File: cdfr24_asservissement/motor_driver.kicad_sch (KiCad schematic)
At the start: 14 parts

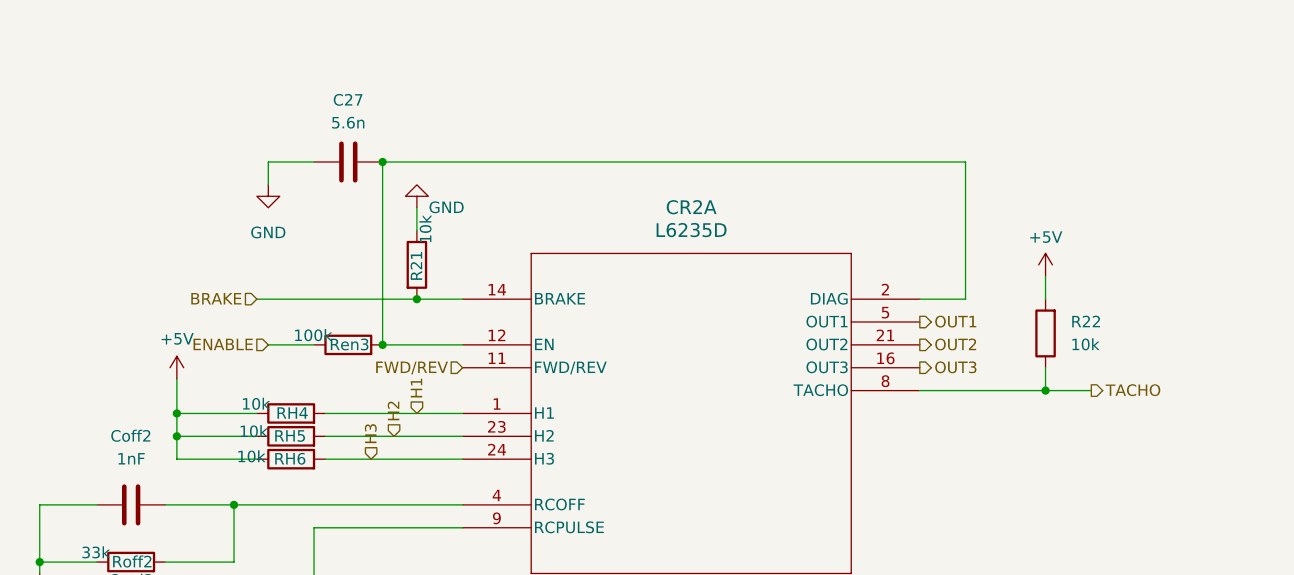
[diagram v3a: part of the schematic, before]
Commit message: Change STM32 pins
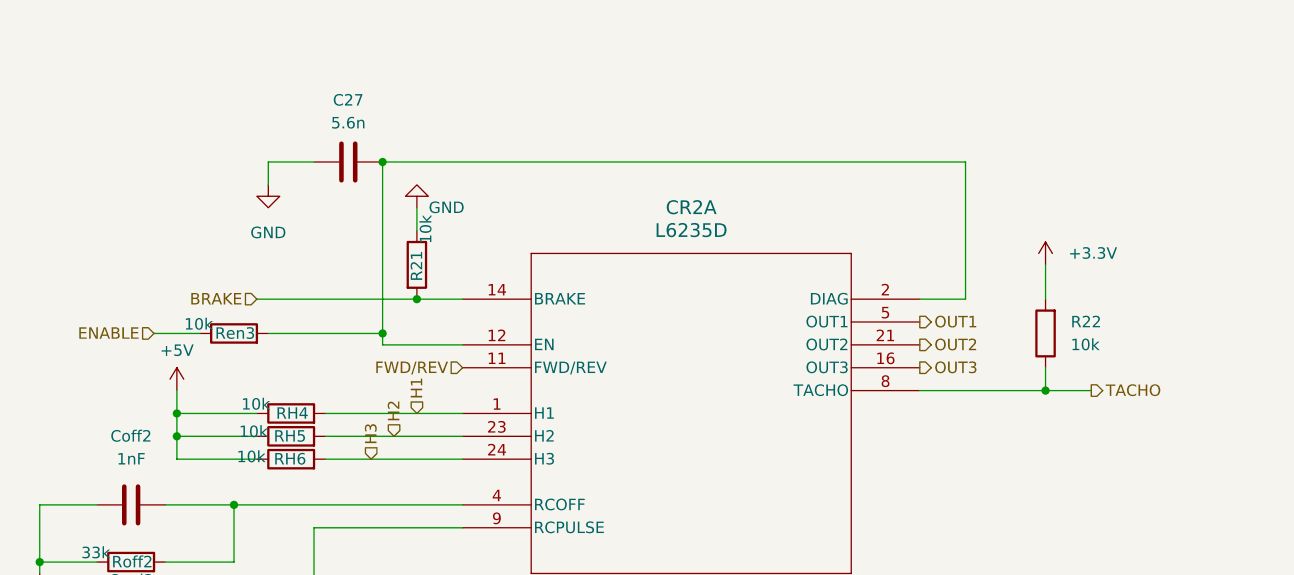
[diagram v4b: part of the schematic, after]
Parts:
- Ren3: value 100k -> 10k
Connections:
- net +5V: no longer R22.2
- new net +3.3V: R22.2
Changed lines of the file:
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@@
-	)
-	(junction
-		(at 120.65 105.41)
-		(diameter 0)
-		(color 0 0 0 0)
 	)
 	(junction
@@
 	)
 	(junction
+		(at 120.65 104.14)
+		(diameter 0)
+		(color 0 0 0 0)
+	)
+	(junction
 		(at 104.14 138.43)
 		(diameter 0)
@@
 	(wire
 		(pts
+			(xy 120.65 104.14) (xy 120.65 105.41)
+		)
+		(stroke
+			(width 0)
+			(type default)
+		)
+	)
+	(wire
+		(pts
 			(xy 104.14 129.54) (xy 96.52 129.54)
 		)
@@
 	(wire
 		(pts
-			(xy 120.65 85.09) (xy 120.65 105.41)
+			(xy 120.65 85.09) (xy 120.65 104.14)
 		)
 		(stroke
@@
 	(wire
 		(pts
-			(xy 107.95 105.41) (xy 113.03 105.41)
-		)
-		(stroke
-			(width 0)
-			(type default)
-		)
-	)
-	(wire
-		(pts
-			(xy 194.31 97.79) (xy 194.31 100.33)
+			(xy 95.25 104.14) (xy 100.33 104.14)
+		)
+		(stroke
+			(width 0)
+			(type default)
+		)
+	)
+	(wire
+		(pts
+			(xy 194.31 96.52) (xy 194.31 100.33)
 		)
 		(stroke
@@
 	(wire
 		(pts
-			(xy 97.79 109.22) (xy 97.79 113.03)
+			(xy 97.79 110.49) (xy 97.79 113.03)
 		)
 		(stroke
@@
 		(pts
 			(xy 106.68 115.57) (xy 97.79 115.57)
+		)
+		(stroke
+			(width 0)
+			(type default)
+		)
+	)
+	(wire
+		(pts
+			(xy 107.95 104.14) (xy 120.65 104.14)
 		)
 		(stroke
@@
 	(hierarchical_label "ENABLE"
 		(shape input)
-		(at 107.95 105.41 180)
+		(at 95.25 104.14 180)
 		(fields_autoplaced yes)
 		(effects
@@
 	)
 	(symbol
+		(lib_id "power:+3.3V")
+		(at 194.31 96.52 0)
+		(unit 1)
+		(exclude_from_sim no)
+		(in_bom yes)
+		(on_board yes)
+		(dnp no)
+		(fields_autoplaced yes)
+		(property "Reference" "#PWR052"
+			(at 194.31 100.33 0)
+			(effects
+				(font
+					(size 1.27 1.27)
+				)
+				(hide yes)
+			)
+		)
+		(property "Value" "+3.3V"
+			(at 196.85 95.2499 0)
+			(effects
+				(font
+					(size 1.27 1.27)
+				)
+				(justify left)
+			)
+		)
+		(property "Footprint" ""
+			(at 194.31 96.52 0)
+			(effects
+				(font
+					(size 1.27 1.27)
+				)
+				(hide yes)
+			)
+		)
+		(property "Datasheet" ""
+			(at 194.31 96.52 0)
+			(effects
+				(font
+					(size 1.27 1.27)
+				)
+				(hide yes)
+			)
+		)
+		(property "Description" ""
+			(at 194.31 96.52 0)
+			(effects
+				(font
+					(size 1.27 1.27)
+				)
+				(hide yes)
+			)
+		)
+		(pin "1"
+		)
+		(instances
+			(project "cdfr24_asservissement"
+				(path "/c6b82269-16f5-49e6-8b51-4d12a40a3077/084e419c-7880-44c5-a0d2-721d5e789f19"
+					(reference "#PWR052")
+					(unit 1)
+				)
+				(path "/c6b82269-16f5-49e6-8b51-4d12a40a3077/fbaa2c7d-8eee-479f-b1be-bb54414743c2"
+					(reference "#PWR046")
+					(unit 1)
+				)
+			)
+		)
+	)
+	(symbol
 		(lib_id "power:GND")
 		(at 107.95 87.63 0)
@@
 	(symbol
 		(lib_id "Device:R")
+		(at 104.14 104.14 90)
+		(unit 1)
+		(exclude_from_sim no)
+		(in_bom yes)
+		(on_board yes)
+		(dnp no)
+		(property "Reference" "Ren3"
+			(at 104.267 104.14 90)
+			(effects
+				(font
+					(size 1.27 1.27)
+				)
+			)
+		)
+		(property "Value" "10k"
+			(at 100.203 103.124 90)
+			(effects
+				(font
+					(size 1.27 1.27)
+				)
+			)
+		)
+		(property "Footprint" "Resistor_SMD:R_0805_2012Metric_Pad1.20x1.40mm_HandSolder"
+			(at 104.14 105.918 90)
+			(effects
+				(font
+					(size 1.27 1.27)
+				)
+				(hide yes)
+			)
+		)
+		(property "Datasheet" "~"
+			(at 104.14 104.14 0)
+			(effects
+				(font
+					(size 1.27 1.27)
+				)
+				(hide yes)
+			)
+		)
+		(property "Description" ""
+			(at 104.14 104.14 0)
+			(effects
+				(font
+					(size 1.27 1.27)
+				)
+				(hide yes)
+			)
+		)
+		(pin "1"
+		)
+		(pin "2"
+		)
+		(instances
+			(project "cdfr24_asservissement"
+				(path "/c6b82269-16f5-49e6-8b51-4d12a40a3077/084e419c-7880-44c5-a0d2-721d5e789f19"
+					(reference "Ren3")
+					(unit 1)
+				)
+				(path "/c6b82269-16f5-49e6-8b51-4d12a40a3077/fbaa2c7d-8eee-479f-b1be-bb54414743c2"
+					(reference "Ren2")
+					(unit 1)
+				)
+			)
+		)
+	)
+	(symbol
+		(lib_id "Device:R")
 		(at 92.71 144.78 90)
 		(unit 1)
@@
 	(symbol
 		(lib_id "power:+5V")
-		(at 194.31 97.79 0)
+		(at 97.79 110.49 0)
 		(unit 1)
 		(exclude_from_sim no)
@@
 		(dnp no)
 		(fields_autoplaced yes)
-		(property "Reference" "#PWR059"
-			(at 194.31 101.6 0)
+		(property "Reference" "#PWR060"
+			(at 97.79 114.3 0)
 			(effects
 				(font
@@
 		)
 		(property "Value" "+5V"
-			(at 194.31 93.472 0)
+			(at 97.79 106.045 0)
 			(effects
 				(font
@@
 		)
 		(property "Footprint" ""
-			(at 194.31 97.79 0)
+			(at 97.79 110.49 0)
 			(effects
 				(font
@@
 		)
 		(property "Datasheet" ""
-			(at 194.31 97.79 0)
+			(at 97.79 110.49 0)
 			(effects
 				(font
@@
 		)
 		(property "Description" ""
-			(at 194.31 97.79 0)
-			(effects
-				(font
-					(size 1.27 1.27)
-				)
-				(hide yes)
-			)
-		)
-		(pin "1"
-		)
-		(instances
-			(project "cdfr24_asservissement"
-				(path "/c6b82269-16f5-49e6-8b51-4d12a40a3077/084e419c-7880-44c5-a0d2-721d5e789f19"
-					(reference "#PWR059")
-					(unit 1)
-				)
-				(path "/c6b82269-16f5-49e6-8b51-4d12a40a3077/fbaa2c7d-8eee-479f-b1be-bb54414743c2"
-					(reference "#PWR046")
-					(unit 1)
-				)
-			)
-		)
-	)
-	(symbol
-		(lib_id "Device:R")
-		(at 116.84 105.41 90)
-		(unit 1)
-		(exclude_from_sim no)
-		(in_bom yes)
-		(on_board yes)
-		(dnp no)
-		(property "Reference" "Ren3"
-			(at 116.967 105.41 90)
-			(effects
-				(font
-					(size 1.27 1.27)
-				)
-			)
-		)
-		(property "Value" "100k"
-			(at 112.903 104.394 90)
-			(effects
-				(font
-					(size 1.27 1.27)
-				)
-			)
-		)
-		(property "Footprint" "Resistor_SMD:R_0805_2012Metric_Pad1.20x1.40mm_HandSolder"
-			(at 116.84 107.188 90)
-			(effects
-				(font
-					(size 1.27 1.27)
-				)
-				(hide yes)
-			)
-		)
-		(property "Datasheet" "~"
-			(at 116.84 105.41 0)
-			(effects
-				(font
-					(size 1.27 1.27)
-				)
-				(hide yes)
-			)
-		)
-		(property "Description" ""
-			(at 116.84 105.41 0)
-			(effects
-				(font
-					(size 1.27 1.27)
-				)
-				(hide yes)
-			)
-		)
-		(pin "1"
-		)
-		(pin "2"
-		)
-		(instances
-			(project "cdfr24_asservissement"
-				(path "/c6b82269-16f5-49e6-8b51-4d12a40a3077/084e419c-7880-44c5-a0d2-721d5e789f19"
-					(reference "Ren3")
-					(unit 1)
-				)
-				(path "/c6b82269-16f5-49e6-8b51-4d12a40a3077/fbaa2c7d-8eee-479f-b1be-bb54414743c2"
-					(reference "Ren2")
-					(unit 1)
-				)
-			)
-		)
-	)
-	(symbol
-		(lib_id "power:+5V")
-		(at 97.79 109.22 0)
-		(unit 1)
-		(exclude_from_sim no)
-		(in_bom yes)
-		(on_board yes)
-		(dnp no)
-		(fields_autoplaced yes)
-		(property "Reference" "#PWR060"
-			(at 97.79 113.03 0)
-			(effects
-				(font
-					(size 1.27 1.27)
-				)
-				(hide yes)
-			)
-		)
-		(property "Value" "+5V"
-			(at 97.79 104.775 0)
-			(effects
-				(font
-					(size 1.27 1.27)
-				)
-			)
-		)
-		(property "Footprint" ""
-			(at 97.79 109.22 0)
-			(effects
-				(font
-					(size 1.27 1.27)
-				)
-				(hide yes)
-			)
-		)
-		(property "Datasheet" ""
-			(at 97.79 109.22 0)
-			(effects
-				(font
-					(size 1.27 1.27)
-				)
-				(hide yes)
-			)
-		)
-		(property "Description" ""
-			(at 97.79 109.22 0)
-			(effects
-				(font
+			(at 97.79 110.49 0)
+			(effects
+				(font

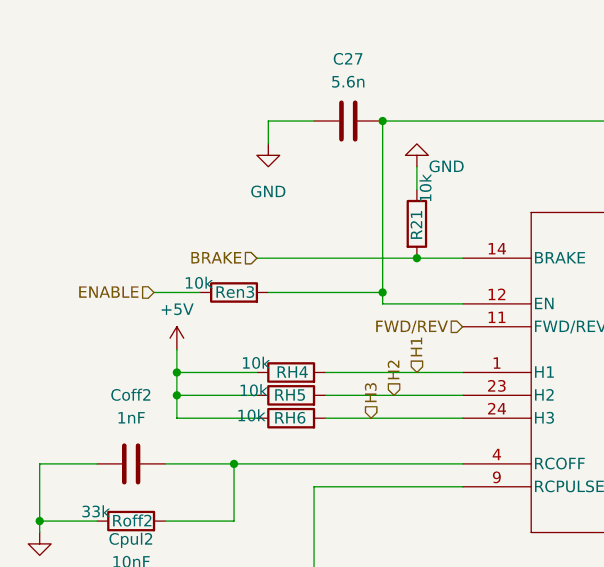
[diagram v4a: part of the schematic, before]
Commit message: Add low pass filter
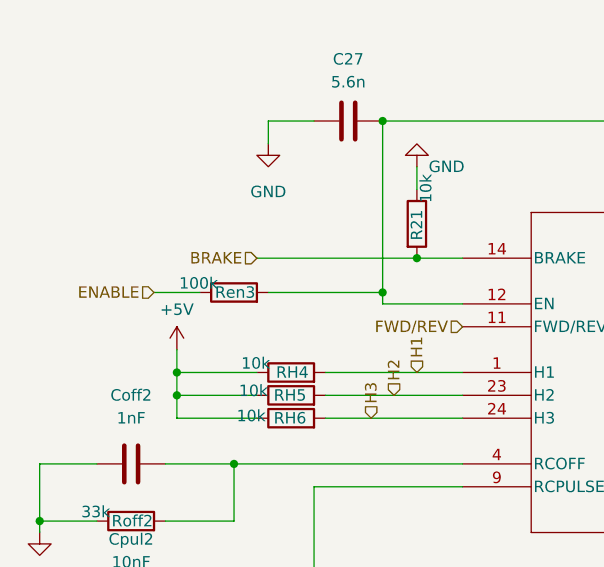
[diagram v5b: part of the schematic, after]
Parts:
- Ren3: value 10k -> 100k
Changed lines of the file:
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@@
 			)
 		)
-		(property "Value" "10k"
+		(property "Value" "100k"
 			(at 100.203 103.124 90)
 			(effects

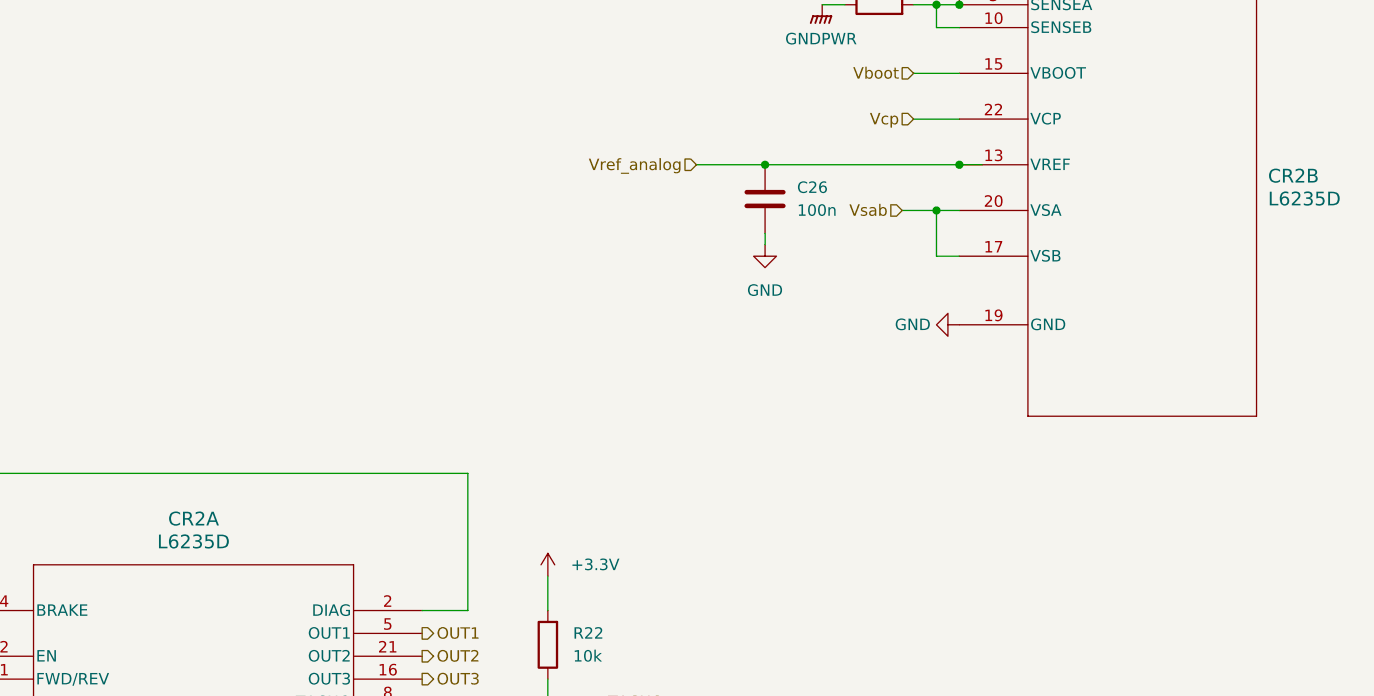
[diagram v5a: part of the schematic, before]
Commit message: Fix warnings, add DIP switches
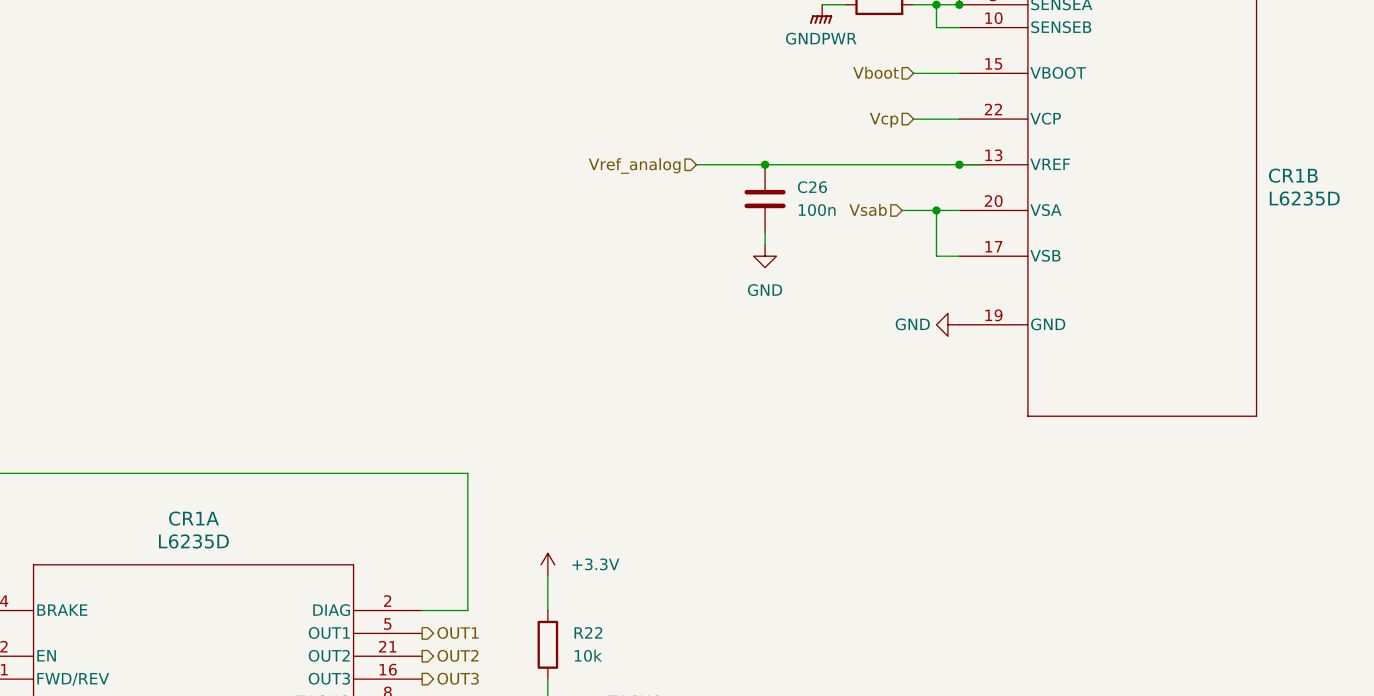
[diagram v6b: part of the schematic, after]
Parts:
- removed CR2: L6235D, L6235D:SO-24_STM, symbol L6235D:L6235D
- added CR1: L6235D, L6235D:SO-24_STM, symbol L6235:L6235D
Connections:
- net BRAKE: now also CR1.14 (BRAKE)
- net FWD/REV: now also CR1.11 (FWD/REV)
- net GND: now also CR1.18 (GND), CR1.19 (GND), CR1.6 (GND), CR1.7 (GND)
- net H1: now also CR1.1 (H1)
- net H2: now also CR1.23 (H2)
- net H3: now also CR1.24 (H3)
- net OUT1: now also CR1.5 (OUT1)
- net OUT2: now also CR1.21 (OUT2)
- net OUT3: now also CR1.16 (OUT3)
- net TACHO: now also CR1.8 (TACHO)
- net Vboot: now also CR1.15 (VBOOT)
- net Vcp: now also CR1.22 (VCP)
- net Vref_analog: now also CR1.13 (VREF)
- net Vsab: now also CR1.17 (VSB), CR1.20 (VSA)
- net at C27.2, Ren3.2: now also CR1.12 (EN), CR1.2 (DIAG)
- net at Coff2.2, Roff2.2: now also CR1.4 (RCOFF)
- net at Cpul2.2, Rpul2.2: now also CR1.9 (RCPULSE)
- net at R11.2: now also CR1.10 (SENSEB), CR1.3 (SENSEA)
